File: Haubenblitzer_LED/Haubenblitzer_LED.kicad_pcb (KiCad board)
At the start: 2 copper layers, 30 x 48.3 mm, 8 parts, among them J1 Conn_01x01_Female, J2 Conn_01x01_Female, J3 Conn_01x01_Female

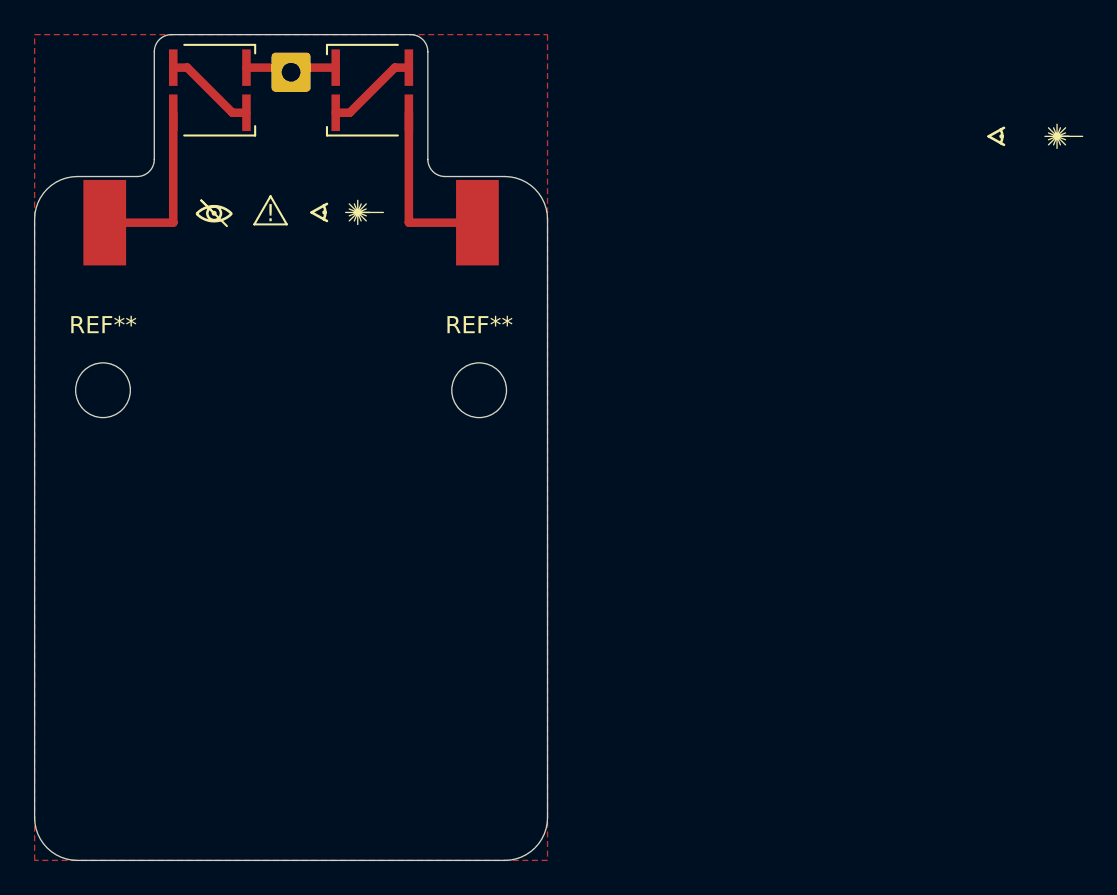
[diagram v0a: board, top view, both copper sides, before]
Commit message: added ESD protection and gerber files
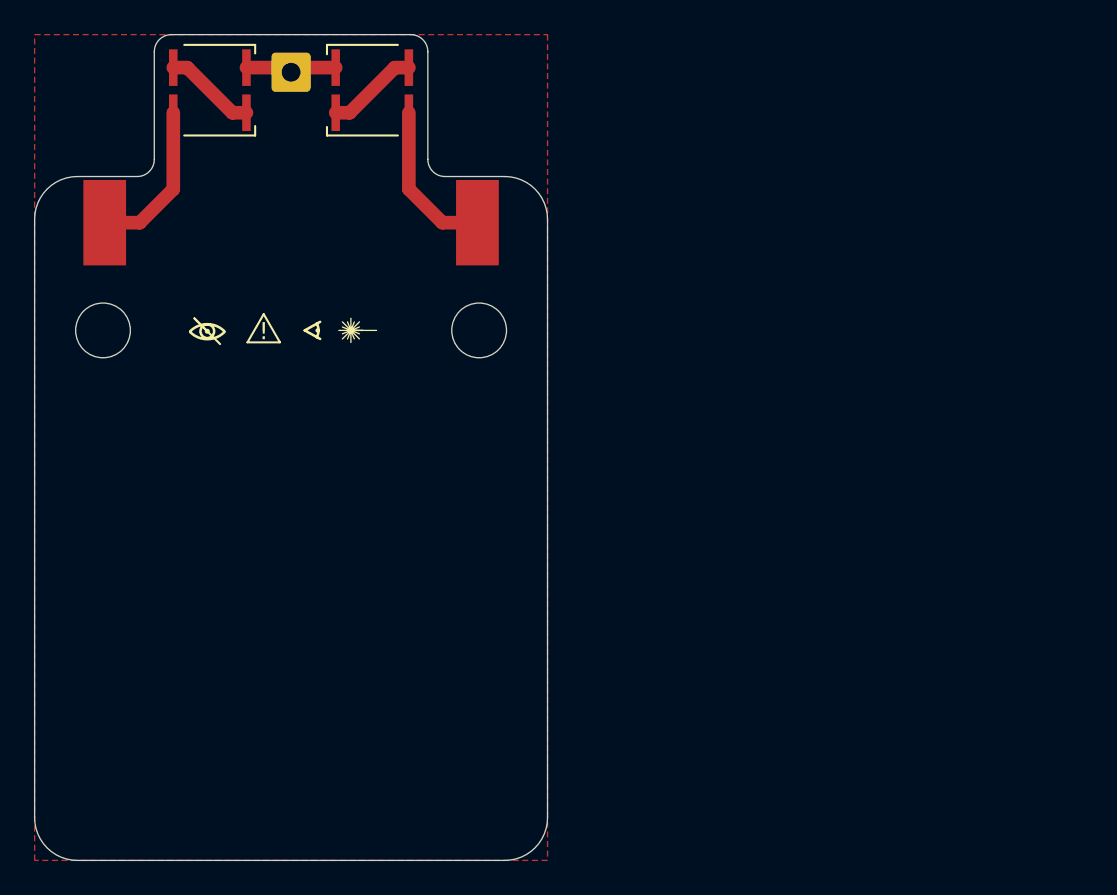
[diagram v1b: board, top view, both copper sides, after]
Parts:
- moved REF** 3.50 mm to (171.5, 123.8)
- moved REF** 3.50 mm to (149.5, 123.8)
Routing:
- net Net-(D2-Pad3): track 10.4 -> 9.29 mm
- net Net-(D1-Pad1): track 10.4 -> 9.29 mm
